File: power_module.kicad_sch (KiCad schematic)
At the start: 0 parts

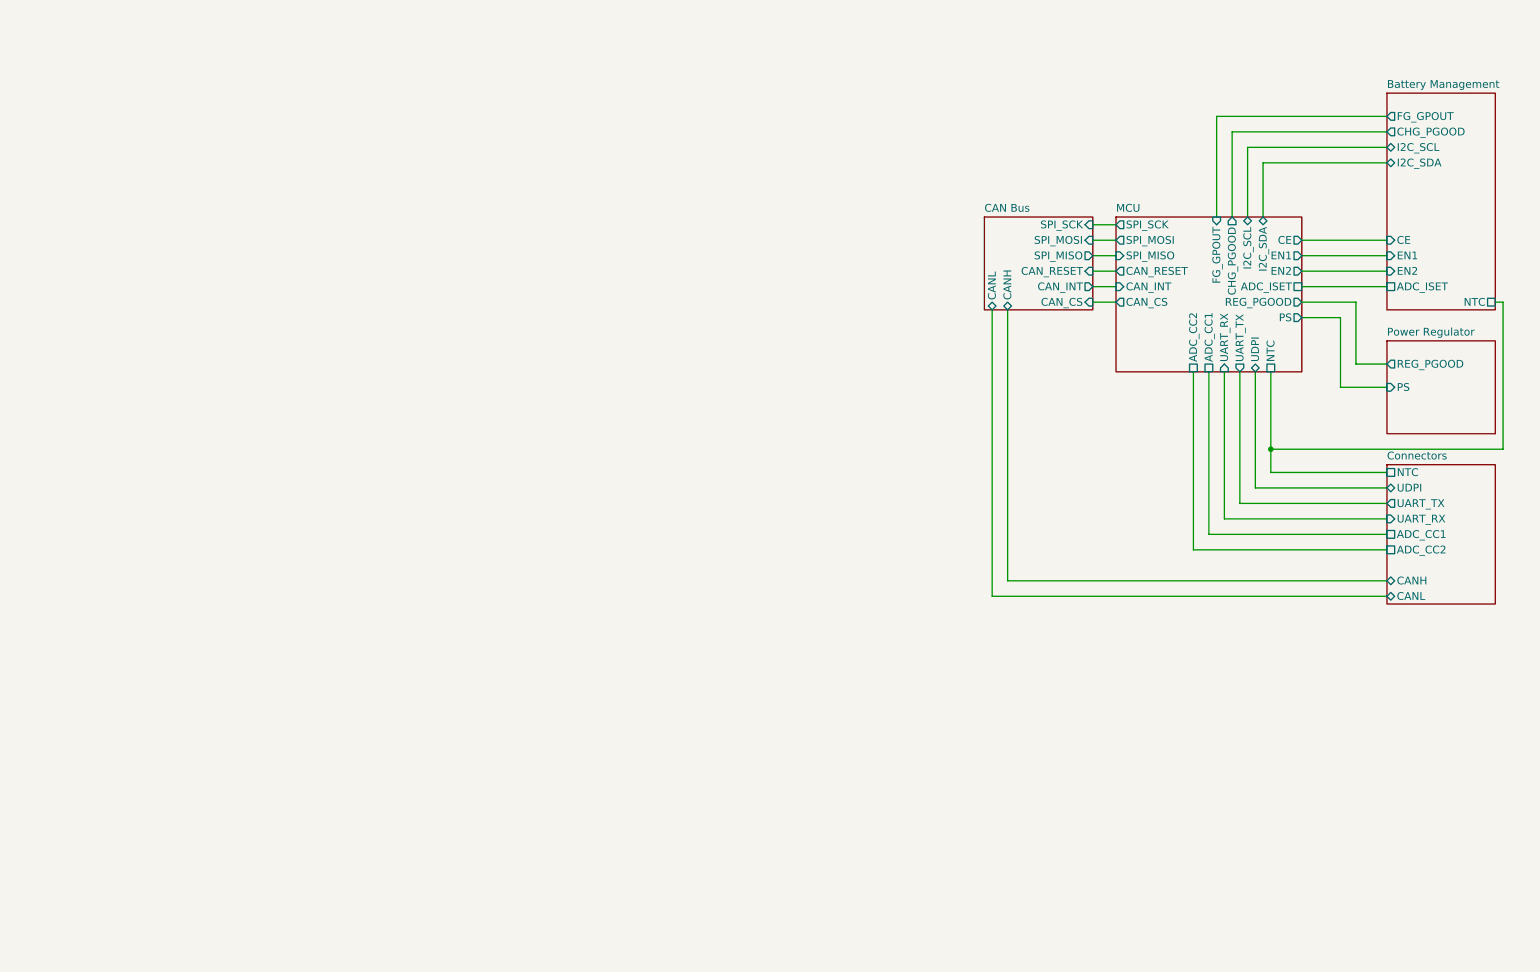
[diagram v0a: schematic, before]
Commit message: Added Graph & cleaned up title and layout
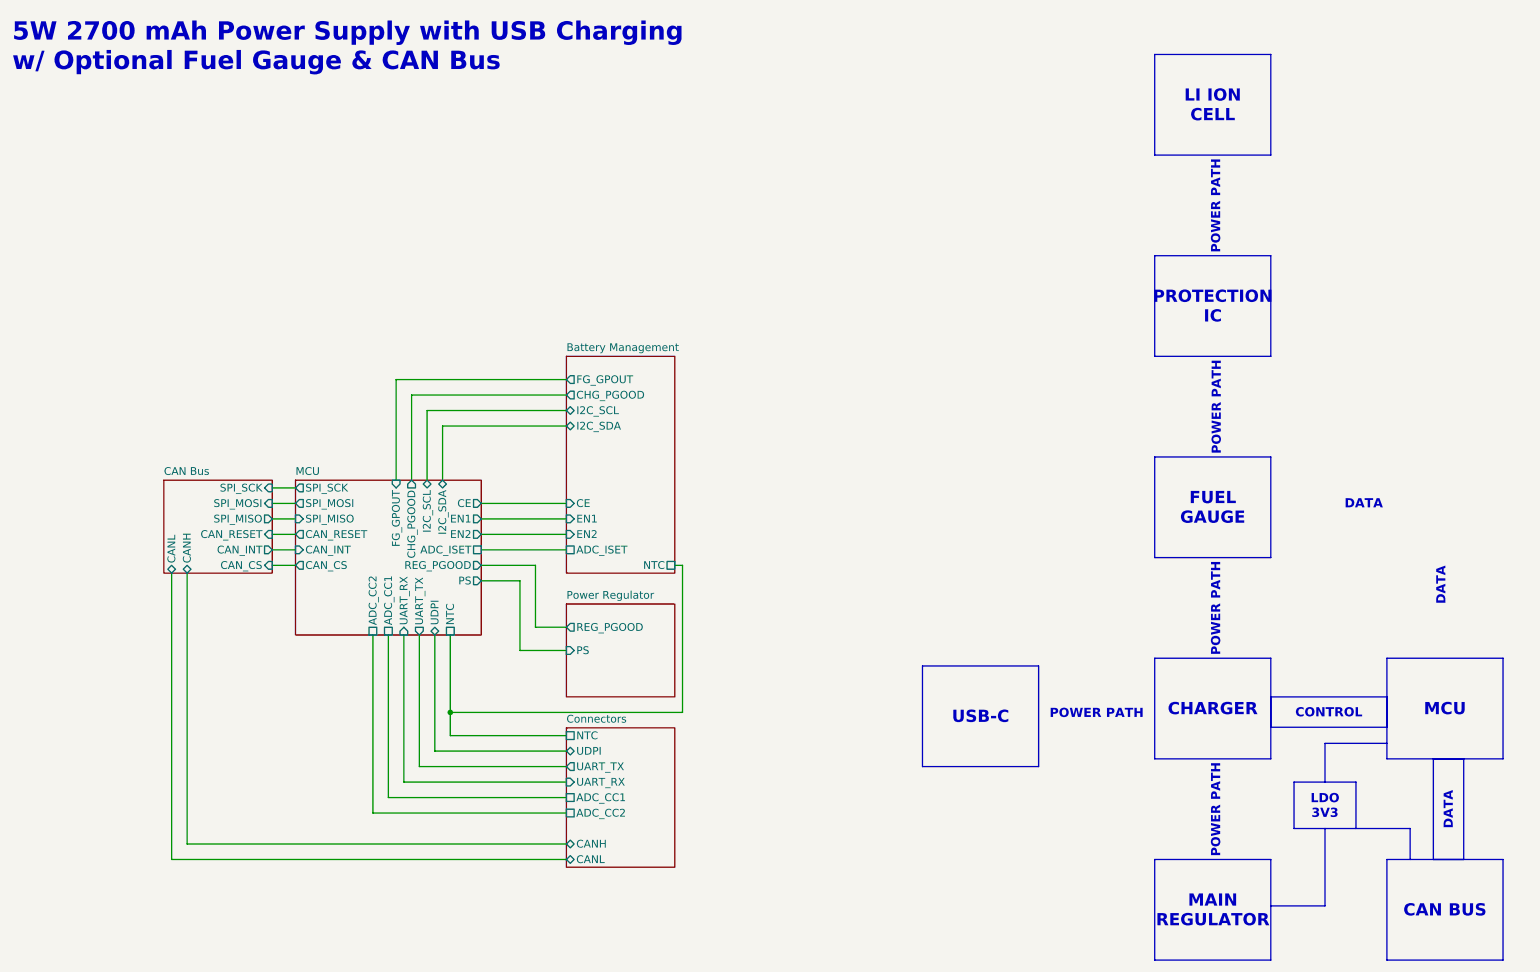
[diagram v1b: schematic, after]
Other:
- note added: "5W 2700 mAh Power Supply with USB Charging w/ Optional Fuel Gauge & CAN Bus"
- company: FETfox -> github.com/FETfox/Li-Ion_Power_Module
- title: Li Lion Power Module -> Li Lion Power Module w/ Optional Fuel Gauge &CAN Bus
